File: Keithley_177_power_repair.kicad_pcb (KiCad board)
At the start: 2 copper layers, 58 x 50 mm, 8 parts, among them T1 RAC20-DK, T101 Transformer, U1 R-78E5.0-1.0

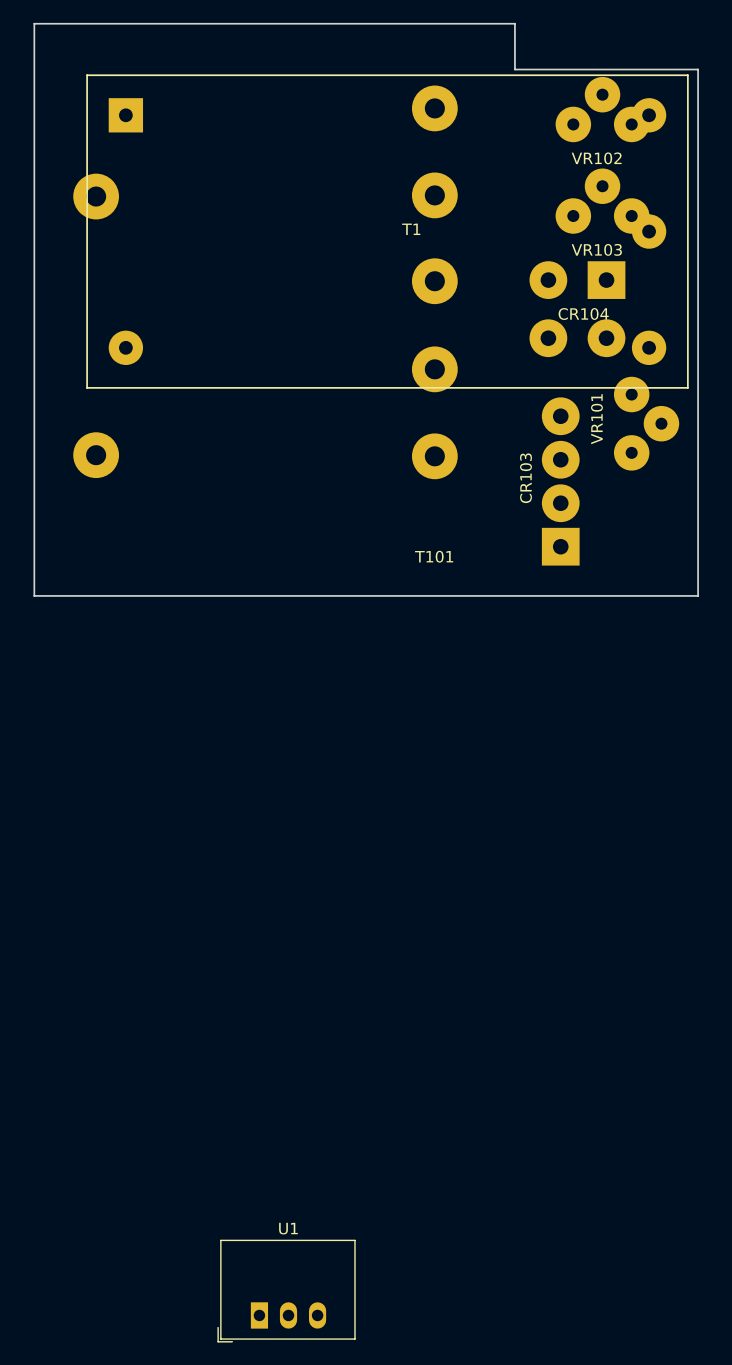
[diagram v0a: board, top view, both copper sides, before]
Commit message: Update Keithley_177_power_repair.kicad_pcb
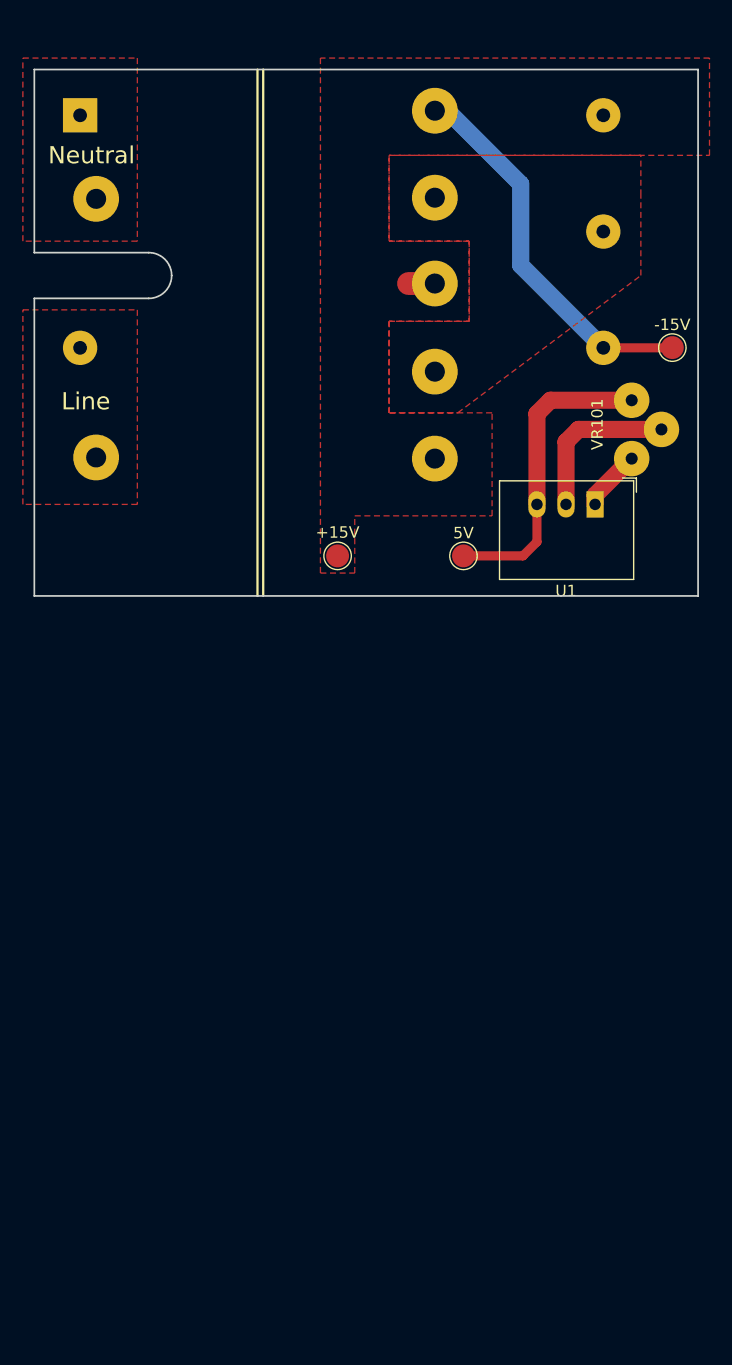
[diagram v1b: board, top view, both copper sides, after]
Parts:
- removed CR103: JUMPERS, Keithley_Components:Bridge_Rectifier_Inline
- removed CR104: JUMPERS, Keithley_Components:Bridge_Rectifier_Square
- removed VR102: L7815, Keithley_Components:Voltage_Regulator
- removed VR103: L7915, Keithley_Components:Voltage_Regulator
- added TP1: +15V, TestPoint:TestPoint_Pad_D2.0mm, F.Cu at (56.5, 86.5)
- added TP2: -15V, TestPoint:TestPoint_Pad_D2.0mm, F.Cu at (85.8, 68.3)
- added TP3: 5V, TestPoint:TestPoint_Pad_D2.0mm, F.Cu at (67.5, 86.5)
- moved U1 76.7 mm to (79.0, 82.0), turned to 180 degrees
- moved T1 4.00 mm to (34.0, 48.0)
- moved VR101 0.50 mm to (82.2, 78.0)
- moved T101 0.20 mm to (65.0, 83.0)
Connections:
- net Net-(T1-Pad4) renamed GND
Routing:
- net -15V: track 0.00 -> 34.1 mm
- net Net-(TP3-Pad1): track 0.00 -> 26.9 mm
- net GNDA: track 0.00 -> 14.3 mm
- net Net-(U1-Pad1): track 0.00 -> 5.33 mm
- net +15V: track 0.00 -> 2.32 mm
- added copper zone on F.Cu, net +15V
- added copper zone on F.Cu, net /L
- added copper zone on F.Cu, net /N
- added copper zone on F.Cu, net GND
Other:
- board size 58 x 50 mm -> 58 x 46 mm
- board text added: "Line"
- board text added: "Neutral"
